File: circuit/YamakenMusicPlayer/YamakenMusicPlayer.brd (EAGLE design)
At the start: 100 x 80 mm, 24 parts, among them J1 DCJ0202, J2 AJ-1780, U1 NJM2396F33, U2 AE-ESP-WROOM-02

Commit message: 表記の修正
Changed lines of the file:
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@@
 <contactref element="U2" pad="P13"/>
 <contactref element="U2" pad="P18"/>
-<contactref element="U$1" pad="GND_2"/>
 <wire x1="78.74" y1="8.89" x2="74.676" y2="8.89" width="0.762" layer="16"/>
 <wire x1="74.676" y1="8.89" x2="68.58" y2="8.89" width="0.762" layer="16"/>
@@
 <wire x1="27.94" y1="27.94" x2="27.94" y2="25.4" width="0.762" layer="16"/>
 <wire x1="38.1" y1="38.1" x2="27.94" y2="27.94" width="0.762" layer="16"/>
-<wire x1="53.086" y1="16.51" x2="40.64" y2="4.064" width="0.762" layer="16"/>
-<wire x1="53.086" y1="17.526" x2="53.086" y2="16.51" width="0.762" layer="16"/>
-<wire x1="53.086" y1="17.526" x2="53.34" y2="17.78" width="0.762" layer="16"/>
 <wire x1="23.114" y1="52.07" x2="23.114" y2="63.246" width="0.762" layer="16"/>
 <wire x1="37.338" y1="37.846" x2="23.114" y2="52.07" width="0.762" layer="16"/>
@@
 <vertex x="55.88" y="40.64"/>
 </polygon>
+<contactref element="U$1" pad="GND_2"/>
+<wire x1="40.64" y1="4.064" x2="53.34" y2="16.764" width="0.762" layer="16"/>
+<wire x1="53.34" y1="16.764" x2="53.34" y2="17.78" width="0.762" layer="16"/>
 </signal>
 <signal name="N$1">

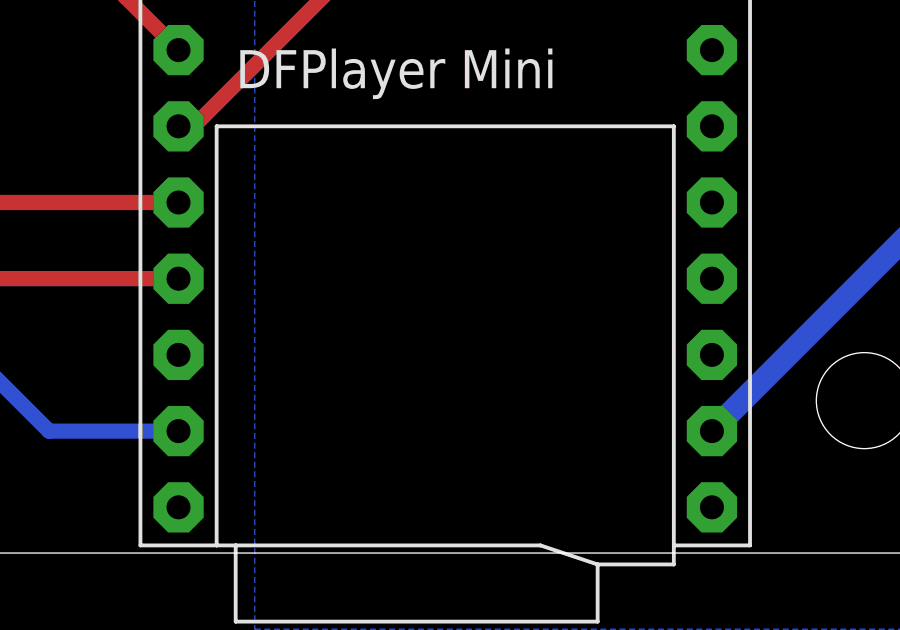
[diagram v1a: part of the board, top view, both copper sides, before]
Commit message: U3の表記を追加
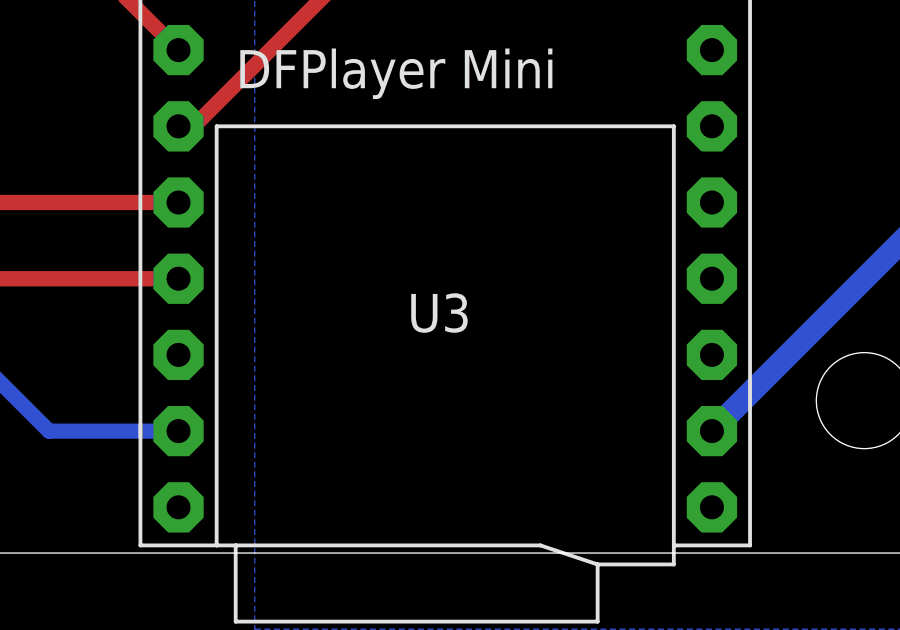
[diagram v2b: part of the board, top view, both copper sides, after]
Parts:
- renumbered U$1 to U3
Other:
- board text added: "U3"
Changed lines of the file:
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@@
 <text x="92.456" y="36.576" size="1.016" layer="25">RESET</text>
 <text x="60.706" y="25.146" size="1.016" layer="25">BOOT MODE</text>
+<text x="30.48" y="7.366" size="1.27" layer="25">U3</text>
 </plain>
 <attributes>
@@
 <attribute name="VALUE" x="85.852" y="5.08" size="1.27" layer="27" ratio="10"/>
 </element>
-<element name="U$1" library="DFPlayer_v1" package="DFPLAYERMINI" value="DFPLAYERMINI" x="31.75" y="10.414" smashed="yes"/>
+<element name="U3" library="DFPlayer_v1" package="DFPLAYERMINI" value="DFPLAYERMINI" x="31.75" y="10.414" smashed="yes"/>
 <element name="U1" library="SamacSys_Parts" package="TO254P480X1000X1900-4P" value="NJM2396F33" x="20.32" y="73.66" smashed="yes">
 <attribute name="DESCRIPTION" value="LOW DROPOUT VOLTAGE REGULATOR WITH ON/OFF CONTROL" x="43.18" y="-12.7" size="1.778" layer="27" display="off"/>
@@
 <contactref element="R2" pad="2"/>
 <contactref element="U2" pad="P1"/>
-<contactref element="U$1" pad="VCC"/>
+<contactref element="U3" pad="VCC"/>
 <wire x1="22.86" y1="25.4" x2="22.86" y2="22.86" width="0.762" layer="1"/>
 <wire x1="55.626" y1="22.86" x2="56.896" y2="22.86" width="0.762" layer="1"/>
@@
 <vertex x="55.88" y="40.64"/>
 </polygon>
-<contactref element="U$1" pad="GND_2"/>
+<contactref element="U3" pad="GND_2"/>
 <wire x1="40.64" y1="4.064" x2="53.34" y2="16.764" width="0.762" layer="16"/>
 <wire x1="53.34" y1="16.764" x2="53.34" y2="17.78" width="0.762" layer="16"/>
@@
 <signal name="PLAYER_TX">
 <contactref element="U2" pad="P14"/>
-<contactref element="U$1" pad="RX"/>
+<contactref element="U3" pad="RX"/>
 <wire x1="82.042" y1="38.1" x2="82.55" y2="38.1" width="0.508" layer="1"/>
 <wire x1="75.692" y1="44.45" x2="82.042" y2="38.1" width="0.508" layer="1"/>
@@
 <signal name="PLAYER_RX">
 <contactref element="U2" pad="P10"/>
-<contactref element="U$1" pad="TX"/>
+<contactref element="U3" pad="TX"/>
 <wire x1="76.962" y1="27.94" x2="82.55" y2="27.94" width="0.508" layer="16"/>
 <wire x1="76.2" y1="27.178" x2="76.962" y2="27.94" width="0.508" layer="16"/>
@@
 </signal>
 <signal name="DAC_R">
-<contactref element="U$1" pad="DAC_R"/>
+<contactref element="U3" pad="DAC_R"/>
 <contactref element="J2" pad="R_1"/>
 <wire x1="10.414" y1="11.684" x2="22.86" y2="11.684" width="0.508" layer="1"/>
@@
 </signal>
 <signal name="DAC_L">
-<contactref element="U$1" pad="DAC_L"/>
+<contactref element="U3" pad="DAC_L"/>
 <contactref element="J2" pad="L_1"/>
 <wire x1="9.144" y1="9.144" x2="22.86" y2="9.144" width="0.508" layer="1"/>
@@
 </signal>
 <signal name="DAC_GND">
-<contactref element="U$1" pad="GND_1"/>
+<contactref element="U3" pad="GND_1"/>
 <contactref element="J2" pad="GND"/>
 <wire x1="18.542" y1="4.064" x2="22.86" y2="4.064" width="0.508" layer="16"/>

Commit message: ファイルの差し替え
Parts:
- J1: value DCJ0202 -> MJ-179PH
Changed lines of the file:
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@@
 <attribute name="VALUE" x="32.639" y="22.987" size="1.27" layer="27" ratio="10" rot="R180"/>
 </element>
-<element name="J1" library="con-jack" library_urn="urn:adsk.eagle:library:154" package="DCJ0202" package3d_urn="urn:adsk.eagle:package:7491/1" value="DCJ0202" x="10.16" y="71.12" smashed="yes" rot="R270">
+<element name="J1" library="con-jack" library_urn="urn:adsk.eagle:library:154" package="DCJ0202" package3d_urn="urn:adsk.eagle:package:7491/1" value="MJ-179PH" x="10.16" y="71.12" smashed="yes" rot="R270">
 <attribute name="MF" value="" x="-1.27" y="1.27" size="1.778" layer="27" rot="R270" display="off"/>
 <attribute name="MPN" value="" x="-1.27" y="1.27" size="1.778" layer="27" rot="R270" display="off"/>

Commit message: 基板の修正
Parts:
- J2: value AJ-1780 -> PG203J; device SamacSys_Parts:AJ-1780 -> con-hirschmann:PG203J
- moved R2 34.5 mm to (38.1, 50.8), turned to 90 degrees
- moved R5 27.0 mm to (38.1, 35.6), turned to 90 degrees
- moved R3 7.18 mm to (55.9, 45.7), turned to 180 degrees
- moved J2 7.11 mm to (7.62, 10.2)
- moved JP2 5.68 mm to (43.2, 43.2)
- moved C3 5.08 mm to (66.0, 48.3), flipped to the bottom, turned to 90 degrees
- moved C4 5.08 mm to (68.6, 50.8), turned to 270 degrees
- moved C5 5.08 mm to (71.1, 50.8), flipped to the bottom, turned to 270 degrees
- moved R4 3.59 mm to (55.9, 30.5), turned to 90 degrees
- moved LED1 2.54 mm to (78.7, 12.7)
- moved LED2 2.54 mm to (68.6, 12.7)
- moved S3 2.54 mm to (88.9, 12.7)
- moved JP1 1.30 mm to (91.7, 30.5)
- turned S1 to 90 degrees
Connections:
- removed net DAC_L: J2.L_1, U3.DAC_L
- new net N$2: J2.5, U3.DAC_L
- net DAC_GND: now also J2.1; no longer J2.GND
- net DAC_R: now also J2.2; no longer J2.R_1
- net N$1: now also U2.P17
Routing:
- net GND: track 249.0 -> 0.00 mm, vias 0 -> 70
- net N$12: track 39.2 -> 10.2 mm
- net DAC_GND: track 23.2 -> 4.32 mm, vias 0 -> 5
- net DAC_L: track 18.6 -> 0.00 mm
- net N$2: track 0.00 -> 18.6 mm
- net PLAYER_TX: track 84.2 -> 69.6 mm
- net PLAYING_LED: track 30.8 -> 40.0 mm
- net N$1: track 17.2 -> 25.4 mm
- net VOLUME: track 46.8 -> 40.4 mm
- net N$4: track 12.6 -> 6.35 mm
- net ONLINE_LED: track 31.4 -> 36.5 mm
- net PLAY_BTN: track 35.2 -> 39.6 mm
- net N$5: track 17.6 -> 19.1 mm
- net V+: track 175.3 -> 176.4 mm, vias 1 -> 0
- net DAC_R: track 14.4 -> 13.8 mm
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- added copper zone on layer 1, net DAC_GND
- added copper zone on layer 16, net DAC_GND
- added copper zone on layer 1, net GND
